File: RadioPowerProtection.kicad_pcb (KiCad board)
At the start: 2 copper layers, 46 x 11 mm, 16 parts, among them Q1 IRF4905, Q2 IRF4905, Q3 Q_PNP_BCE

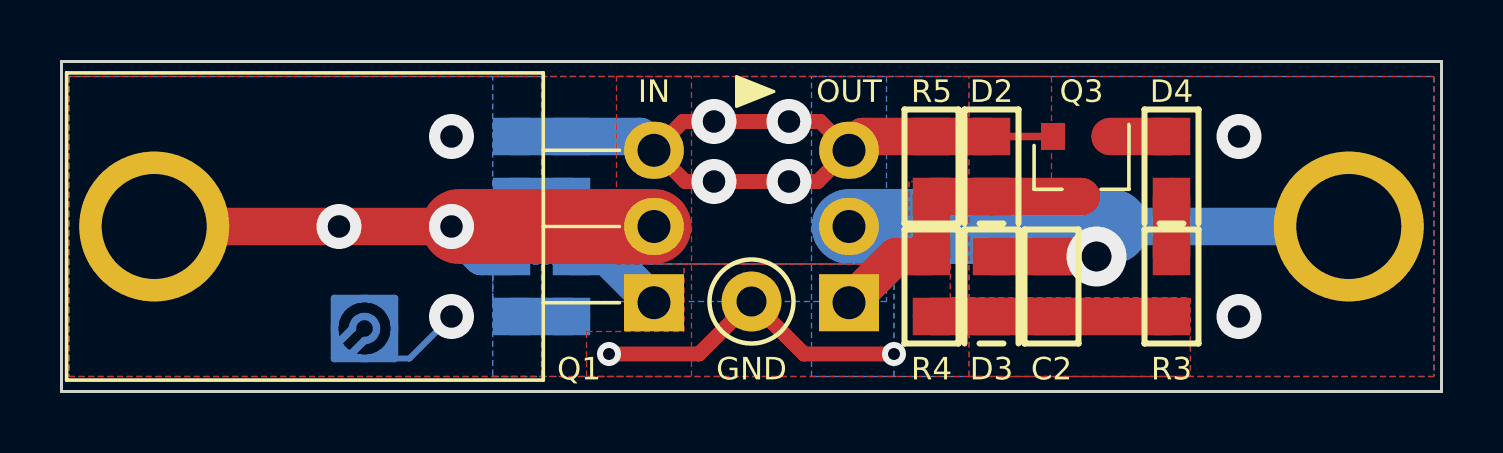
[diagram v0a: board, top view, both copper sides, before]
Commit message: Fix PNP transistor
Signed-off-by: Andres Gongora <mail@andresgongora.com>
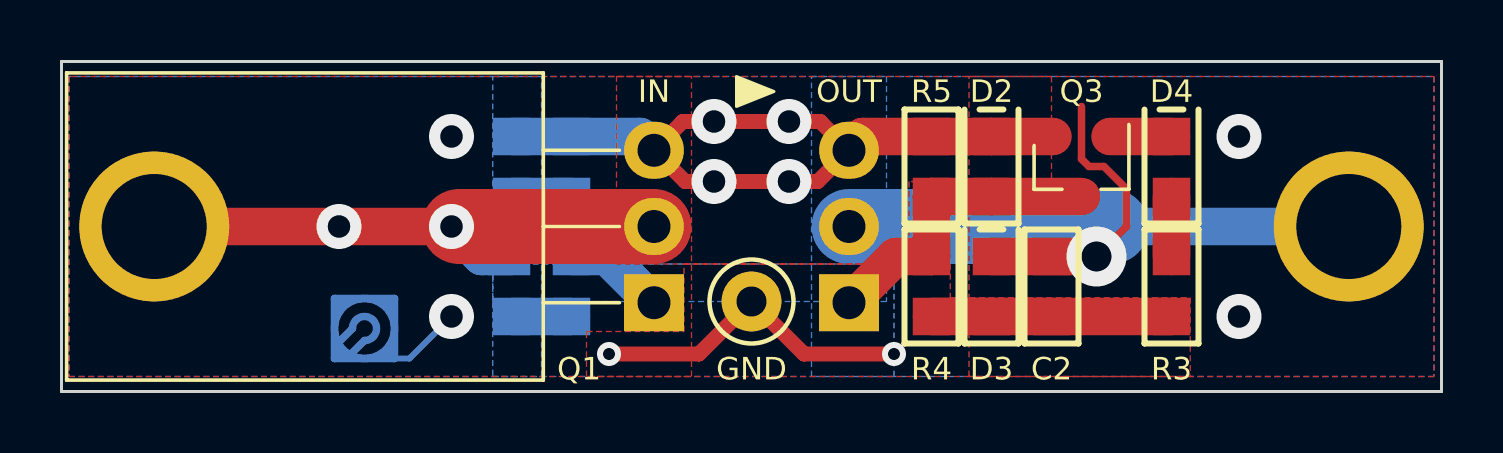
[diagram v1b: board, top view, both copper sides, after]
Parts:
- turned D1 to 0 degrees
- turned D2 to 180 degrees
- turned D3 to 180 degrees
- turned D4 to 180 degrees
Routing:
- net PowerOut: track 20.2 -> 26.5 mm
